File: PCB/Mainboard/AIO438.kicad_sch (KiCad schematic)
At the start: 0 parts

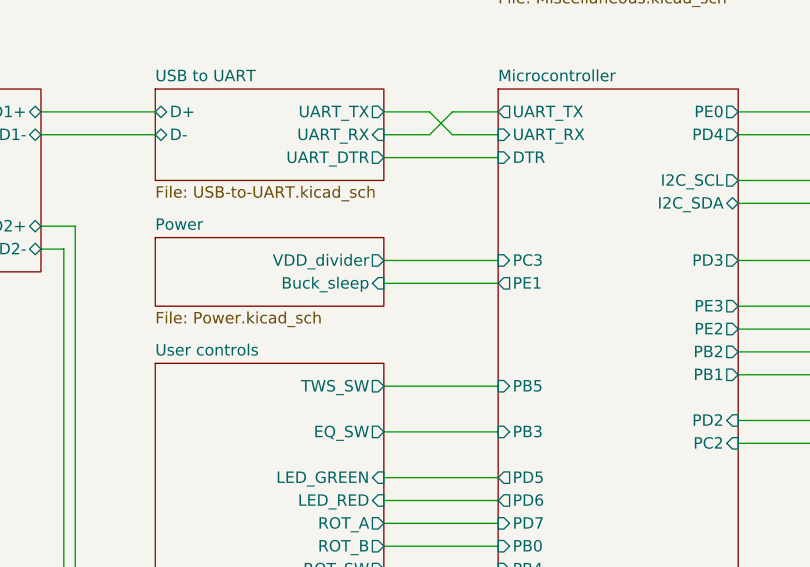
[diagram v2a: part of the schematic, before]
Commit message: Add buck, change some part values
Add new buck in schematic and layout.
Modify BT module footprint,
Change power led resistor from 1k to 100R
Change 4.7u TAS resistors to 10u (consolidation)
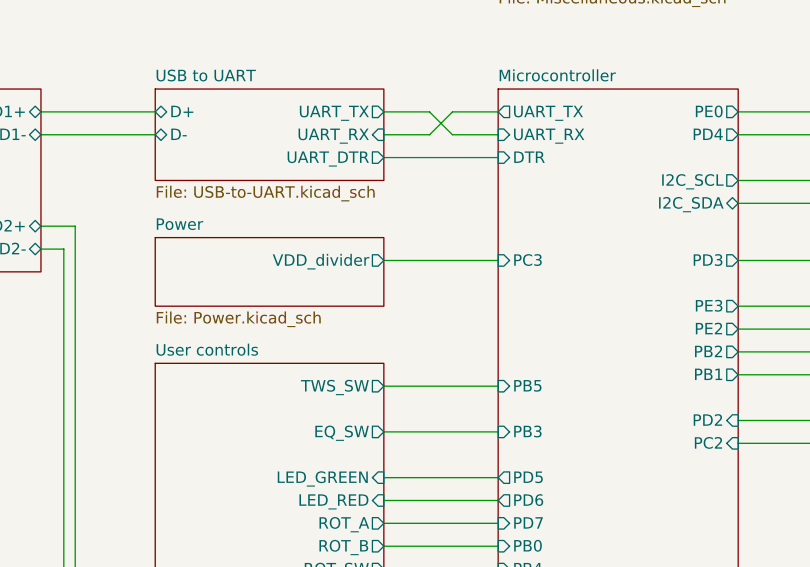
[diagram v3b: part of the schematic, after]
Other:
- sheet Microcontroller ports: added none; removed PE1
- sheet Power ports: added none; removed Buck_sleep
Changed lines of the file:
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@@
-    (stroke (width 0) (type default) (color 0 0 0 0))
-  )
-  (wire (pts (xy 121.92 83.82) (xy 134.62 83.82))
     (stroke (width 0) (type default) (color 0 0 0 0))
   )
@@
       (effects (font (size 1.27 1.27)) (justify right))
     )
-    (pin "Buck_sleep" input (at 121.92 83.82 0)
-      (effects (font (size 1.27 1.27)) (justify right))
-    )
   )
   (sheet (at 173.99 78.74) (size 25.4 64.77) (fields_autoplaced)
@@
     )
     (pin "PC3" input (at 134.62 81.28 180)
-      (effects (font (size 1.27 1.27)) (justify left))
-    )
-    (pin "PE1" output (at 134.62 83.82 180)
       (effects (font (size 1.27 1.27)) (justify left))
     )
@@
       (reference "#PWR0123") (unit 1) (value "GND") (footprint "")
     )
-    (path "/00000000-0000-0000-0000-000060b7ac16/00000000-0000-0000-0000-000061aea057"
+    (path "/00000000-0000-0000-0000-000060b7ac16/4dc68e4f-dbc5-486f-b6b3-ef980cea5397"
       (reference "#PWR0124") (unit 1) (value "GND") (footprint "")
     )
@@
       (reference "#PWR0128") (unit 1) (value "VDD") (footprint "")
     )
-    (path "/00000000-0000-0000-0000-000060b7ac16/00000000-0000-0000-0000-000061b0256d"
+    (path "/00000000-0000-0000-0000-000060b7ac16/41913b4a-48ef-4d73-b0f6-2fde8acc6c2a"
       (reference "#PWR0129") (unit 1) (value "GND") (footprint "")
     )
@@
       (reference "#PWR0134") (unit 1) (value "GND") (footprint "")
     )
-    (path "/00000000-0000-0000-0000-000060b7ac16/00000000-0000-0000-0000-000061af0c5d"
+    (path "/00000000-0000-0000-0000-000060b7ac16/90d2b175-660d-4cb5-a921-803fef4d9e78"
       (reference "#PWR0135") (unit 1) (value "GND") (footprint "")
     )
@@
     )
     (path "/00000000-0000-0000-0000-000060aad6df/00000000-0000-0000-0000-000061d69c28/00000000-0000-0000-0000-000061d73cf4"
-      (reference "C19") (unit 1) (value "4.7u") (footprint "Capacitor_SMD:C_0805_2012Metric")
+      (reference "C19") (unit 1) (value "10u") (footprint "Capacitor_SMD:C_0805_2012Metric")
     )
     (path "/00000000-0000-0000-0000-000060aad6df/00000000-0000-0000-0000-000061d69c28/00000000-0000-0000-0000-000061d73c39"
       (reference "C20") (unit 1) (value "1u") (footprint "Capacitor_SMD:C_0805_2012Metric")
     )
-    (path "/00000000-0000-0000-0000-000060b7ac16/00000000-0000-0000-0000-000060ba49d3"
+    (path "/00000000-0000-0000-0000-000060b7ac16/ab0fe2da-71cb-4c31-9beb-75d40d659007"
       (reference "C21") (unit 1) (value "1u") (footprint "Capacitor_SMD:C_0805_2012Metric")
     )
-    (path "/00000000-0000-0000-0000-000060b7ac16/00000000-0000-0000-0000-000060ba49cd"
-      (reference "C22") (unit 1) (value "1u") (footprint "Capacitor_SMD:C_0805_2012Metric")
+    (path "/00000000-0000-0000-0000-000060b7ac16/d18be9ce-68ba-4a18-9755-e2829c6a9119"
+      (reference "C22") (unit 1) (value "100n") (footprint "Capacitor_SMD:C_0603_1608Metric")
     )
     (path "/00000000-0000-0000-0000-000060b7ac16/00000000-0000-0000-0000-000060c76998"
@@
     )
     (path "/00000000-0000-0000-0000-000060aad6df/00000000-0000-0000-0000-000061db323f/00000000-0000-0000-0000-000061d73cf4"
-      (reference "C57") (unit 1) (value "4.7u") (footprint "Capacitor_SMD:C_0805_2012Metric")
+      (reference "C57") (unit 1) (value "10u") (footprint "Capacitor_SMD:C_0805_2012Metric")
     )
     (path "/00000000-0000-0000-0000-000060aad6df/00000000-0000-0000-0000-000061db323f/00000000-0000-0000-0000-000061d73d33"
@@
       (reference "C60") (unit 1) (value "100n") (footprint "Capacitor_SMD:C_0603_1608Metric")
     )
+    (path "/00000000-0000-0000-0000-000060b7ac16/d36b5d69-e051-4ad3-9459-d144c0ecf55d"
+      (reference "C61") (unit 1) (value "18p") (footprint "Capacitor_SMD:C_0603_1608Metric")
+    )
     (path "/00000000-0000-0000-0000-000060e45fc0/00000000-0000-0000-0000-000060c62fee"
       (reference "D1") (unit 1) (value "Blue") (footprint "LED_SMD:LED_0603_1608Metric")
@@
     )
     (path "/00000000-0000-0000-0000-000060be11e8/00000000-0000-0000-0000-000060be2ad2"
-      (reference "R24") (unit 1) (value "1k") (footprint "Resistor_SMD:R_0603_1608Metric")
+      (reference "R24") (unit 1) (value "100R") (footprint "Resistor_SMD:R_0603_1608Metric")
     )
     (path "/00000000-0000-0000-0000-000060be11e8/00000000-0000-0000-0000-000060be2ae7"
@@
       (reference "R54") (unit 1) (value "1k") (footprint "Resistor_SMD:R_0603_1608Metric")
     )
+    (path "/00000000-0000-0000-0000-000060b7ac16/ad7fc7ce-fa42-453e-a634-b803343fcc44"
+      (reference "R55") (unit 1) (value "100k") (footprint "Resistor_SMD:R_0603_1608Metric")
+    )
+    (path "/00000000-0000-0000-0000-000060b7ac16/3c09aec0-968c-4e16-9609-0ee9ae484e9d"
+      (reference "R56") (unit 1) (value "31k6") (footprint "Resistor_SMD:R_0603_1608Metric")
+    )
+    (path "/00000000-0000-0000-0000-000060bb64c6/fa014d6e-f6aa-4fba-aacb-14cc26eb9152"
+      (reference "TP1") (unit 1) (value "TestPoint") (footprint "TestPoint:TestPoint_Pad_D1.0mm")
+    )
     (path "/00000000-0000-0000-0000-000060aad6df/00000000-0000-0000-0000-000061db323f/00000000-0000-0000-0000-000061a2f14f"
       (reference "U1") (unit 1) (value "TAS5825M") (footprint "zoudio_footprints:TAS5825M")
@@
       (reference "U3") (unit 1) (value "AMS1117-3.3") (footprint "Package_TO_SOT_SMD:SOT-223-3_TabPin2")
     )
-    (path "/00000000-0000-0000-0000-000060b7ac16/00000000-0000-0000-0000-000061ad4d39"
-      (reference "U4") (unit 1) (value "TPS62177") (footprint "zoudio_footprints:WSON-10-1EP_2x3mm_P0.5mm_EP0.84x2.4mm")
+    (path "/00000000-0000-0000-0000-000060b7ac16/755e49a0-7e25-4377-ad3c-4fa4ba141027"
+      (reference "U4") (unit 1) (value "AP63357DV-7") (footprint "zoudio_footprints:V-DFN3020-13")
     )
     (path "/00000000-0000-0000-0000-000060b7ac16/00000000-0000-0000-0000-000061c1f89e"
